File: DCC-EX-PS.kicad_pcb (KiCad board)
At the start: 2 copper layers, 50.8 x 40.6 mm, 9 parts, among them J1 54-00129, J2 OSTVN03A150, U1 TSR 0.5-2450, U2 TSR 2-24120

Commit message: Added QR code to back of the board
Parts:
- added G***: LOGO, DCC-EX-PS:DCC-EX-PS-QR-14x14, B.Cu at (149.9, 72.4)

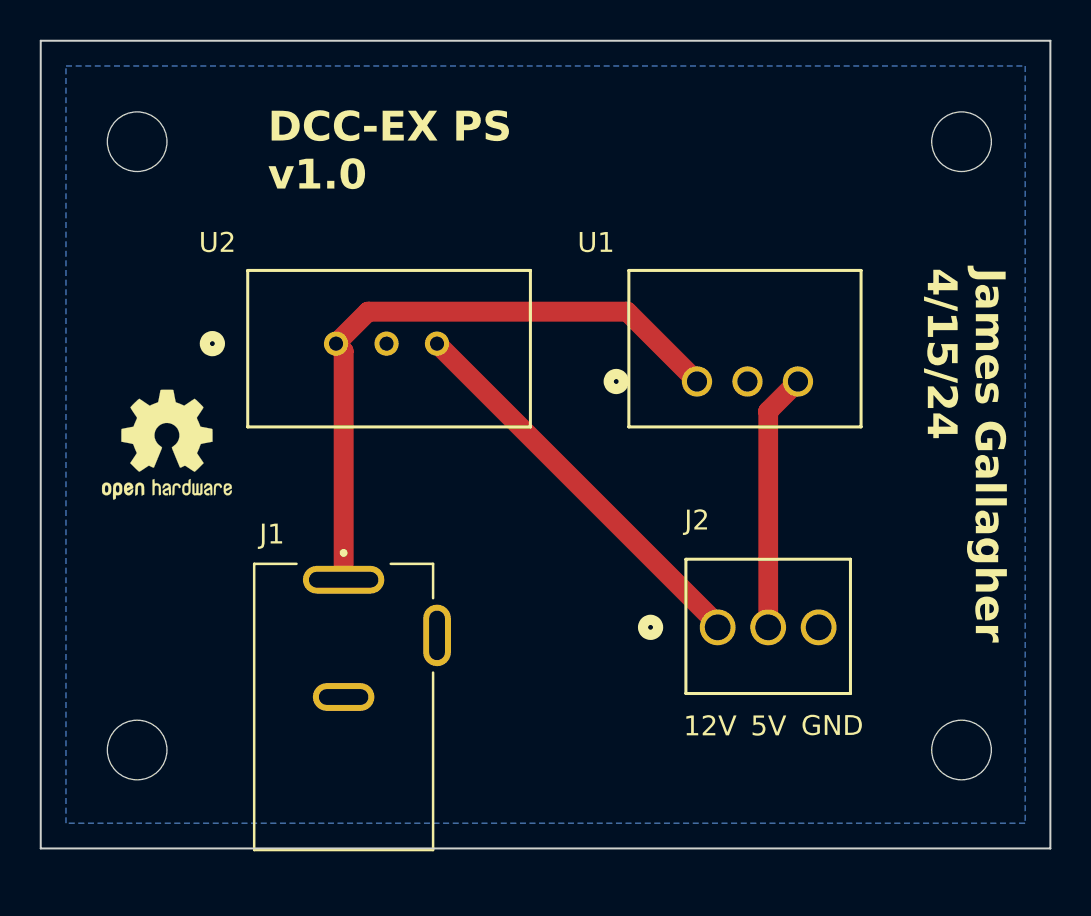
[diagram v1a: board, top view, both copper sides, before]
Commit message: Added more graphics and 24v out terminal
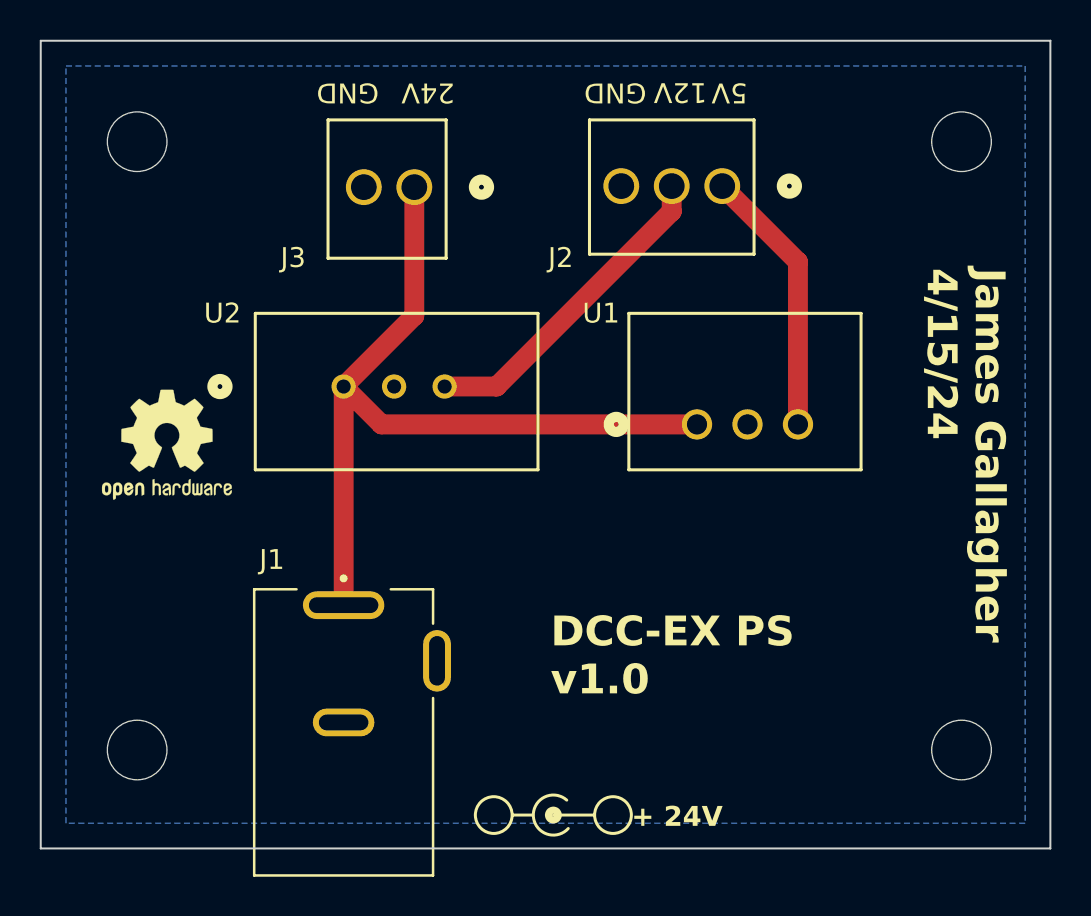
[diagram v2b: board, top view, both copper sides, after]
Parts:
- added J3: OSTVN02A150, DCC-EX-PS:CONN_OSTVN02A150_OST, F.Cu at (135.6, 70.9)
- added REF**: Symbol_Barrel_Polarity, Symbol:Symbol_Barrel_Polarity, F.Cu at (142.6, 102.4)
- moved J2 22.2 mm to (151.1, 70.8), turned to 180 degrees
- moved G*** 21.6 mm to (149.4, 94.0)
- moved U2 2.19 mm to (132.1, 80.9)
- moved U1 2.16 mm to (149.9, 82.8)
- moved J1 1.28 mm to (132.1, 97.8)
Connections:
- J2 pad 1: Net-(U2-+VOUT) -> Net-(U1-+VOUT)
- J2 pad 2: Net-(U1-+VOUT) -> Net-(U2-+VOUT)
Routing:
- net VCC: track 32.3 -> 41.1 mm
- net Net-(U2-+VOUT): track 20.1 -> 16.4 mm
- net Net-(U1-+VOUT): track 13.0 -> 13.6 mm
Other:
- board text added: "+ 24V"
- board text added: "24V"
